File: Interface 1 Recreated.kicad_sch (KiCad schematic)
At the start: 27 parts, among them Q10 BC183, Q11 BC183, U1 LA15-302, U2 TMS4764, U3 74LS260, U4 74HC04, X1 8Mhz

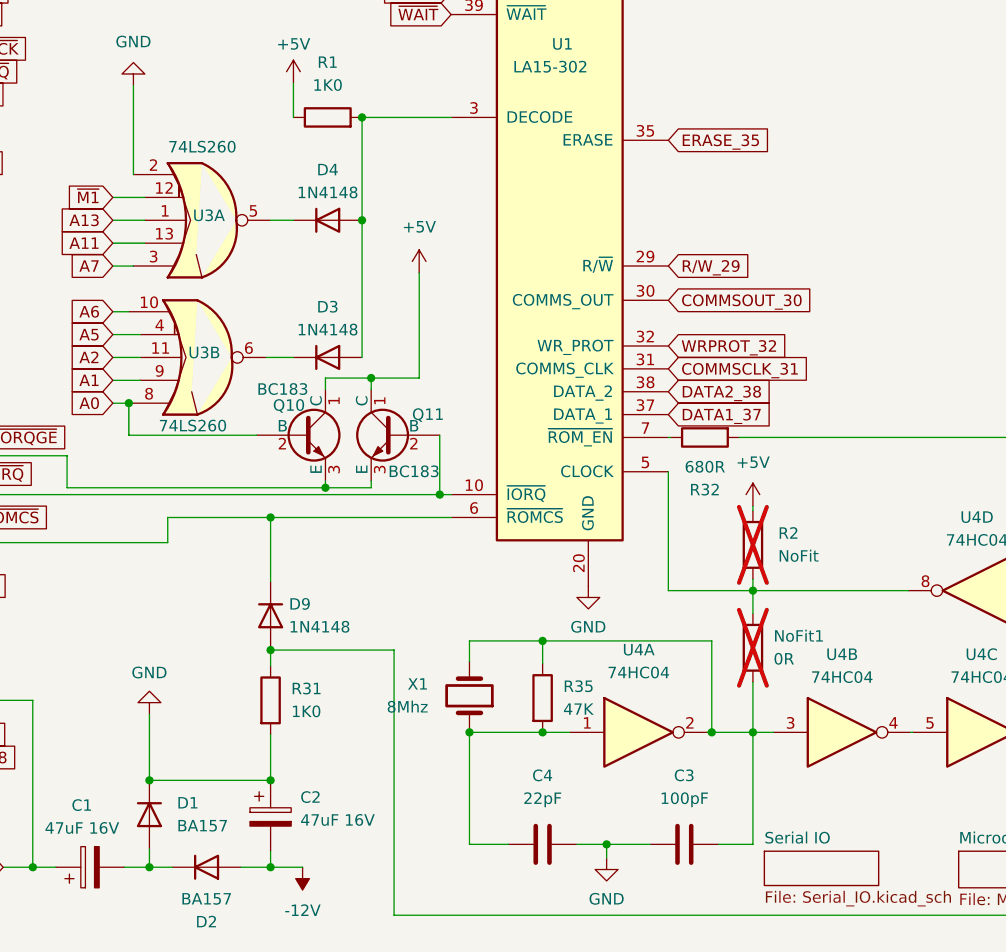
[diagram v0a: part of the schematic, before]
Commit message: Add files via upload
Updated with Kicad 9. Now includes bom/ibom.html (Interactice BOM)
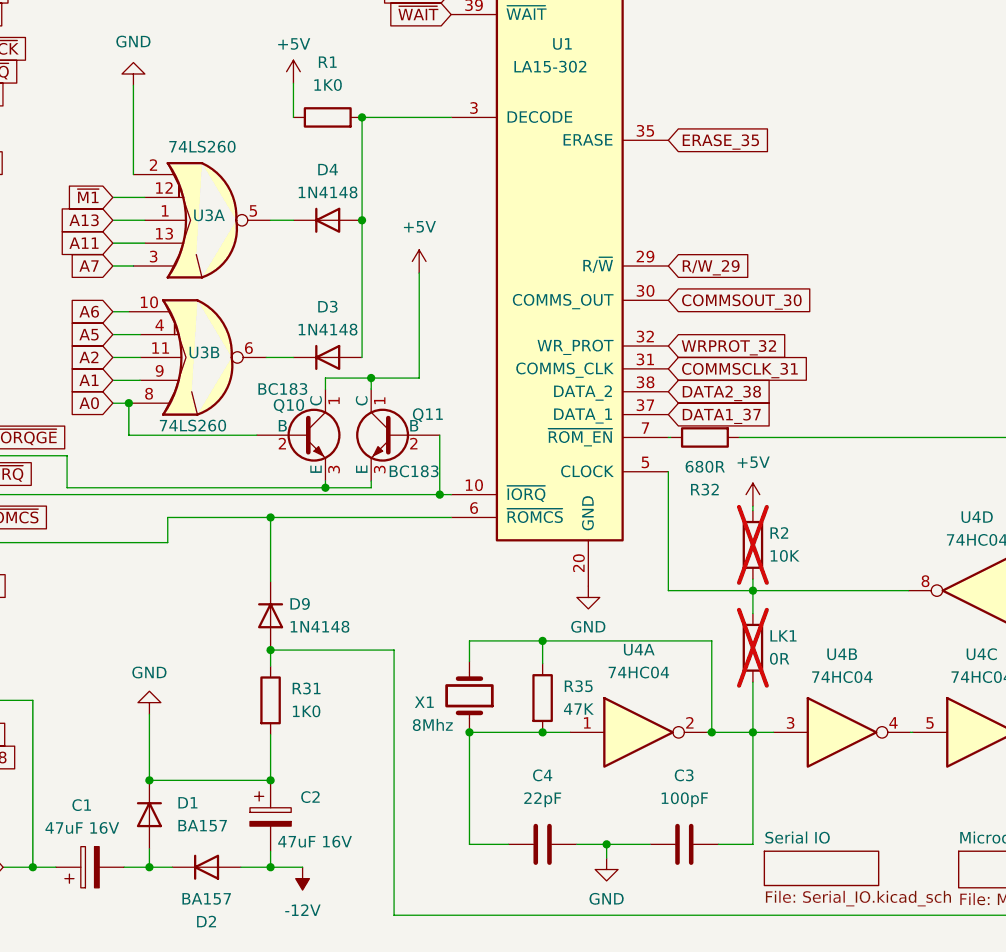
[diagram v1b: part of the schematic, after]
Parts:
- C1, C2, C6: footprint Capacitor_THT:C_Axial_L17.0mm_D6.5mm_P20.00mm_Horizontal -> Mod:C_Axial_L17.0mm_D6.5mm_P20.00mm_Horizontal
- C3, C4: footprint Spectrum:Capacitor Ceramic -> Mod:Capacitor Ceramic
- C5: footprint Capacitor_THT:C_Axial_L3.8mm_D2.6mm_P12.50mm_Horizontal -> Mod:C_Axial_L3.8mm_D2.6mm_P12.50mm_Horizontal
- D1, D10, D2, D3, D4, D9: footprint Spectrum:Diode 1N -> Mod:Diode 1N
- LK1: renamed from NoFit1; footprint Spectrum:Resistor_0.25W -> Mod:Resistor_0.25W
- Q10, Q11: footprint Package_TO_SOT_THT:TO-92L_Inline_Wide -> Mod:TO-92L_Inline_Wide
- R1: footprint ZX Bits:Resistor_0.25W -> Mod:Resistor_0.25W
- R2: value NoFit -> 10K; footprint Spectrum:Resistor_0.25W -> Mod:Resistor_0.25W
- R31, R32, R35: footprint Spectrum:Resistor_0.25W -> Mod:Resistor_0.25W
- SK5: footprint ZX Bits:Spectrum_Edge_Connector -> Mod:Edge_Connector_Up_To_Spectrum; symbol ZXSpectrumPort:Spectrum_port -> IF1_Symbols:Edge_Connector_Up_To_Spectrum
- SK6: footprint ZX Bits:ZX_Bus_Edge_Connector -> Mod:Edge_Connector_To_AddOn; symbol ZXIF1Expansion2:expansion_port_2 -> IF1_Symbols:Edge_Connector_To_AddOn_PCB
- U1: footprint Package_DIP:DIP-40_W15.24mm -> Mod:DIP-40_W15.24mm; symbol LA15-302:LA15-302 -> IF1_Symbols:LA15-302
- U2: footprint Package_DIP:DIP-24_W15.24mm -> Mod:DIP-24_W15.24mm; symbol TMS4764:TMS4764 -> IF1_Symbols:TMS4764
- U3: footprint Package_DIP:DIP-14_W7.62mm -> Mod:DIP-14_W7.62mm; symbol 74LS260:74LS260 -> IF1_Symbols:74LS260
- U4: footprint Package_DIP:DIP-14_W7.62mm -> Mod:DIP-14_W7.62mm
- X1: footprint Crystal:Crystal_HC18-U_Horizontal -> Mod:Crystal_HC18-U_Horizontal
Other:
- company: (none) -> Drawn by liveboxandy
- title: ZX Interface 1 Schematic -> ZX Interface 1 Schematic - Sinclair Labels
